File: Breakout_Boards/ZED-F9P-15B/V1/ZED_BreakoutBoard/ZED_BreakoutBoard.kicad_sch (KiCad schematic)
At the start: 15 parts, among them IC1 ZED-F9P-15B, J1 RF2-04A-T-00-50-G, J2 GPS_Conn_02x04_Top_Bottom

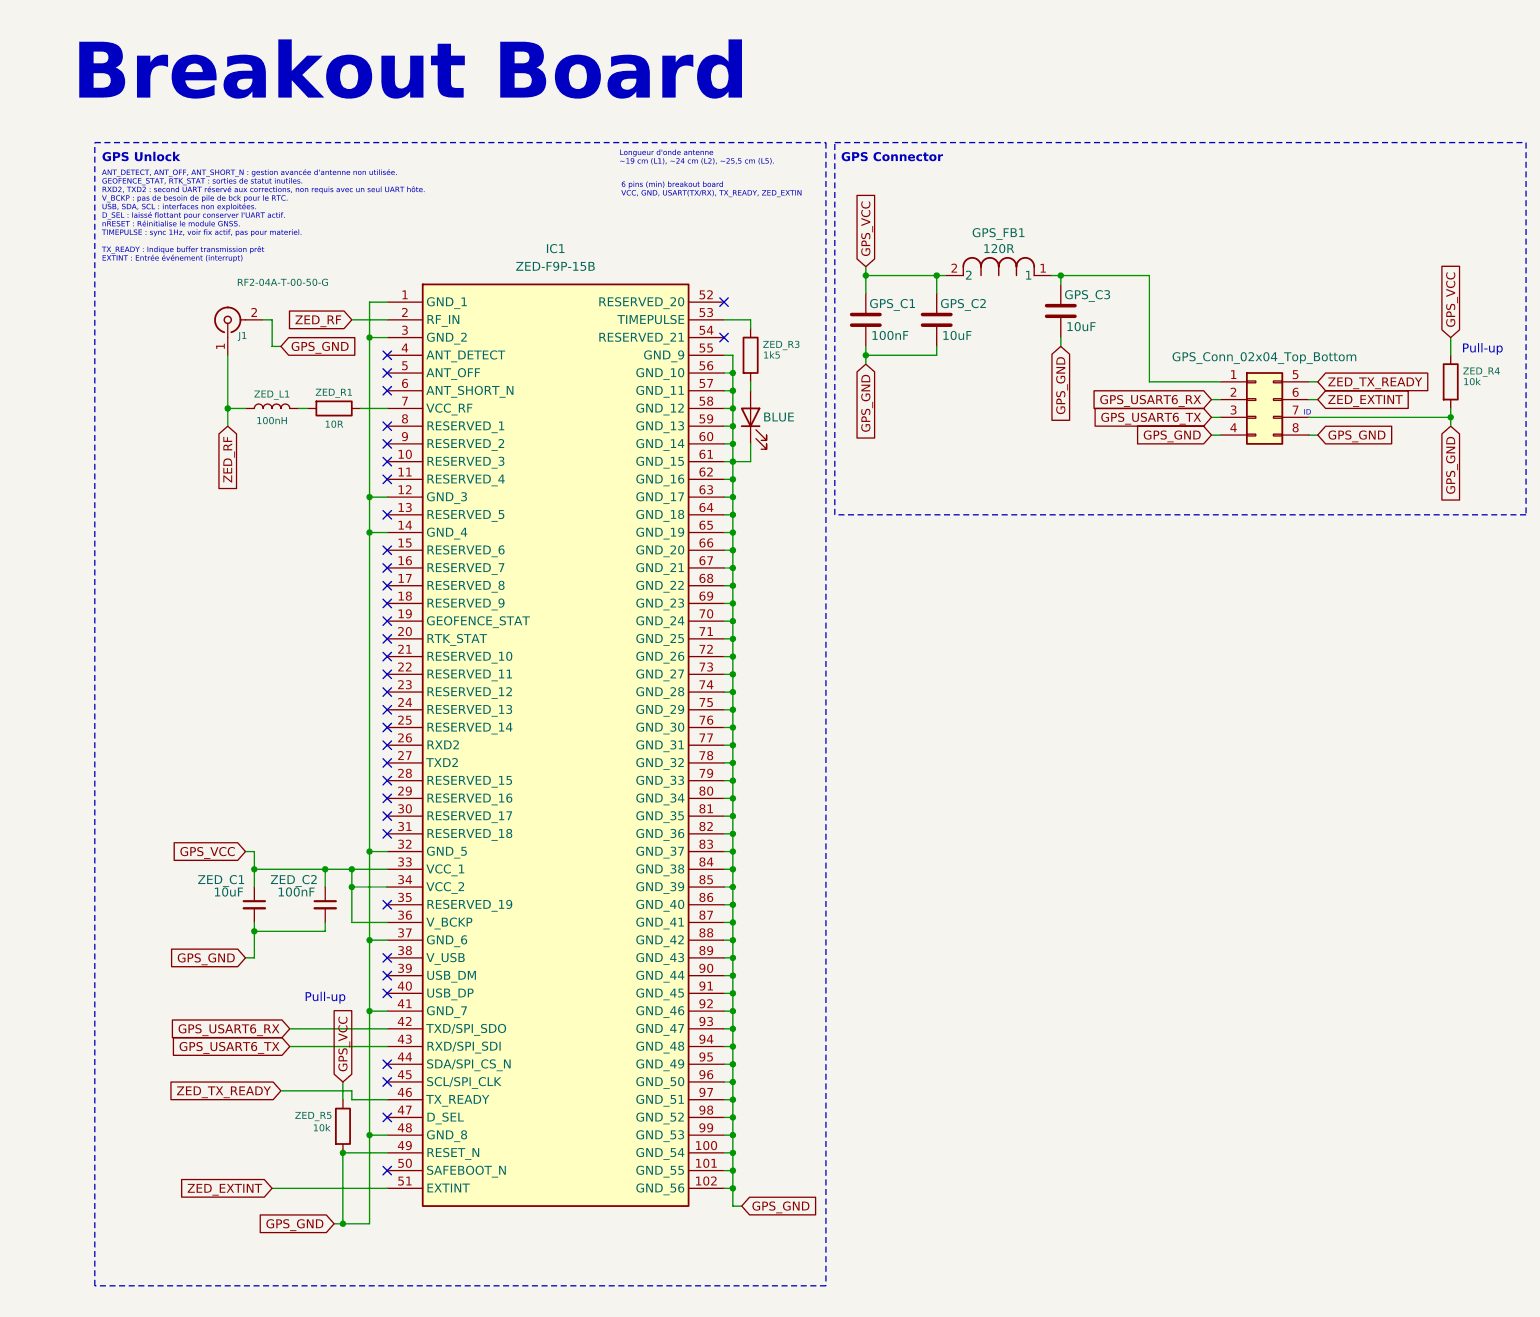
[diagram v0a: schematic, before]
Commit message: fix: pull-up -> 1 logic
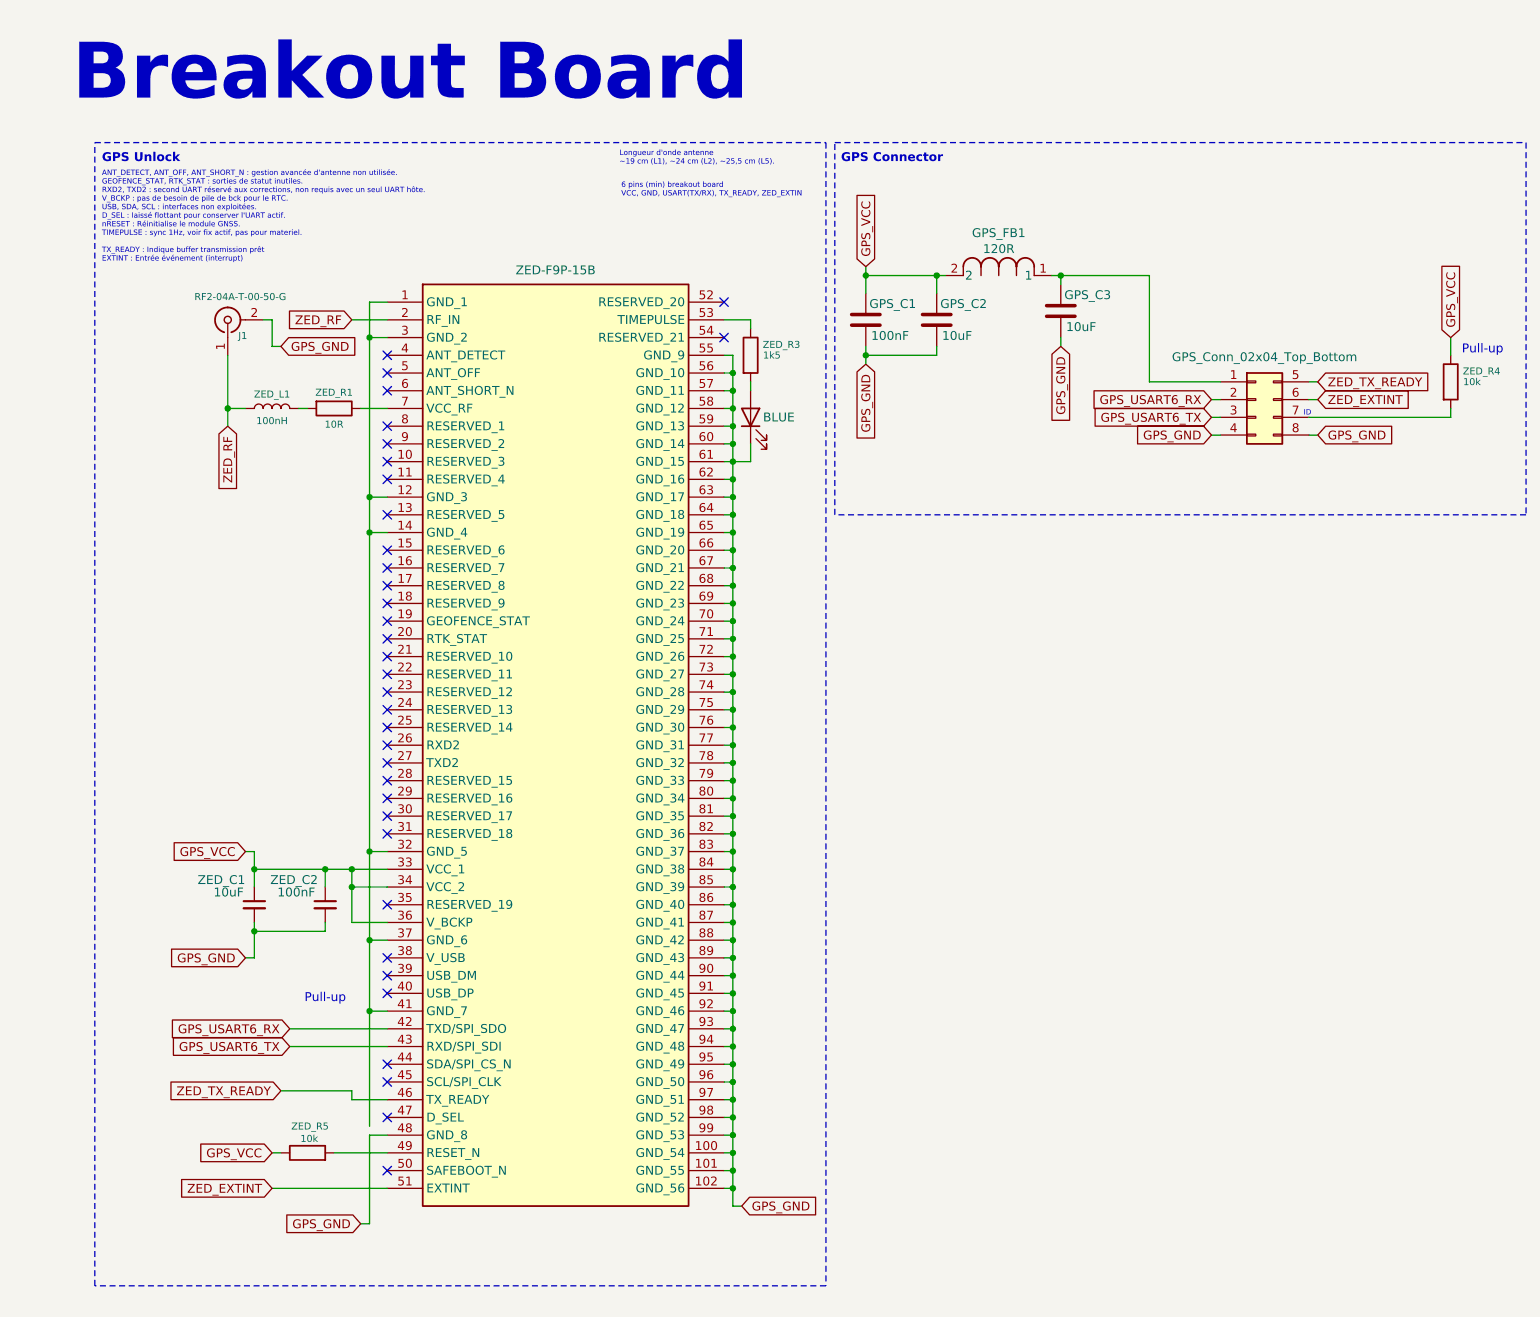
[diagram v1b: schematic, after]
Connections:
- net GPS_GND: no longer IC1.1 (GND_1), IC1.12 (GND_3), IC1.14 (GND_4), IC1.3 (GND_2), IC1.32 (GND_5), IC1.37 (GND_6), IC1.41 (GND_7), IC1.49 (RESET_N), J2.7 (Pin_7), ZED_R4.2, ZED_R5.2
- new net: J2.7 (Pin_7), ZED_R4.2
- new net: IC1.1 (GND_1), IC1.12 (GND_3), IC1.14 (GND_4), IC1.3 (GND_2), IC1.32 (GND_5), IC1.37 (GND_6), IC1.41 (GND_7)
- new net: IC1.49 (RESET_N), ZED_R5.2
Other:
- moved on the sheet: ZED_R5
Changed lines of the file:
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@@
 	)
 	(junction
-		(at 209.55 69.85)
-		(diameter 0)
-		(color 0 0 0 0)
-	)
-	(junction
 		(at 106.68 93.98)
 		(diameter 0)
@@
 	)
 	(junction
-		(at 50.8 185.42)
-		(diameter 0)
-		(color 0 0 0 0)
-	)
-	(junction
 		(at 106.68 180.34)
 		(diameter 0)
@@
 	)
 	(junction
-		(at 50.8 175.26)
-		(diameter 0)
-		(color 0 0 0 0)
-	)
-	(junction
 		(at 106.68 111.76)
 		(diameter 0)
@@
 	)
 	(junction
-		(at 54.61 172.72)
-		(diameter 0)
-		(color 0 0 0 0)
-	)
-	(junction
 		(at 38.1 134.62)
 		(diameter 0)
@@
 	(wire
 		(pts
-			(xy 106.68 73.66) (xy 106.68 76.2)
+			(xy 49.53 175.26) (xy 57.15 175.26)
 		)
 		(stroke
@@
 	(wire
 		(pts
-			(xy 57.15 53.34) (xy 54.61 53.34)
+			(xy 106.68 73.66) (xy 106.68 76.2)
 		)
 		(stroke
@@
 	(wire
 		(pts
-			(xy 125.73 60.96) (xy 125.73 62.23)
+			(xy 57.15 53.34) (xy 54.61 53.34)
 		)
 		(stroke
@@
 	(wire
 		(pts
-			(xy 105.41 96.52) (xy 106.68 96.52)
+			(xy 125.73 60.96) (xy 125.73 62.23)
 		)
 		(stroke
@@
 	(wire
 		(pts
-			(xy 153.67 58.42) (xy 153.67 59.69)
+			(xy 105.41 96.52) (xy 106.68 96.52)
 		)
 		(stroke
@@
 	(wire
 		(pts
-			(xy 54.61 86.36) (xy 54.61 132.08)
+			(xy 153.67 58.42) (xy 153.67 59.69)
 		)
 		(stroke
@@
 	(wire
 		(pts
-			(xy 105.41 127) (xy 106.68 127)
+			(xy 54.61 86.36) (xy 54.61 132.08)
 		)
 		(stroke
@@
 	(wire
 		(pts
-			(xy 50.8 175.26) (xy 50.8 185.42)
+			(xy 105.41 127) (xy 106.68 127)
 		)
 		(stroke
@@
 	(wire
 		(pts
+			(xy 40.64 175.26) (xy 41.91 175.26)
+		)
+		(stroke
+			(width 0)
+			(type default)
+		)
+	)
+	(wire
+		(pts
 			(xy 106.68 177.8) (xy 106.68 180.34)
 		)
@@
 	(wire
 		(pts
-			(xy 54.61 154.94) (xy 54.61 172.72)
+			(xy 54.61 154.94) (xy 54.61 171.45)
 		)
 		(stroke
@@
 	(wire
 		(pts
-			(xy 49.53 185.42) (xy 50.8 185.42)
-		)
-		(stroke
-			(width 0)
-			(type default)
-		)
-	)
-	(wire
-		(pts
 			(xy 43.18 160.02) (xy 57.15 160.02)
 		)
@@
 	(wire
 		(pts
-			(xy 50.8 175.26) (xy 57.15 175.26)
-		)
-		(stroke
-			(width 0)
-			(type default)
-		)
-	)
-	(wire
-		(pts
 			(xy 153.67 49.53) (xy 153.67 50.8)
 		)
@@
 	(wire
 		(pts
-			(xy 50.8 165.1) (xy 50.8 167.64)
-		)
-		(stroke
-			(width 0)
-			(type default)
-		)
-	)
-	(wire
-		(pts
 			(xy 105.41 157.48) (xy 106.68 157.48)
 		)
@@
 	(wire
 		(pts
-			(xy 209.55 69.85) (xy 209.55 71.12)
-		)
-		(stroke
-			(width 0)
-			(type default)
-		)
-	)
-	(wire
-		(pts
 			(xy 106.68 83.82) (xy 106.68 86.36)
 		)
@@
 	(wire
 		(pts
-			(xy 54.61 185.42) (xy 50.8 185.42)
+			(xy 53.34 185.42) (xy 54.61 185.42)
 		)
 		(stroke
@@
 	(global_label "GPS_VCC"
 		(shape input)
-		(at 50.8 165.1 90)
+		(at 40.64 175.26 180)
 		(fields_autoplaced yes)
 		(effects
@@
 				(size 1.27 1.27)
 			)
-			(justify left)
+			(justify right)
 		)
 		(property "Intersheetrefs" "${INTERSHEET_REFS}"
-			(at 50.8 153.7691 90)
+			(at 29.3091 175.26 0)
 			(effects
 				(font
 					(size 1.27 1.27)
 				)
-				(justify left)
+				(justify right)
 				(hide yes)
 			)
@@
 	(global_label "GPS_GND"
 		(shape input)
-		(at 49.53 185.42 180)
+		(at 53.34 185.42 180)
 		(fields_autoplaced yes)
 		(effects
@@
 		)
 		(property "Intersheetrefs" "${INTERSHEET_REFS}"
-			(at 37.9572 185.42 0)
+			(at 41.7672 185.42 0)
 			(effects
 				(font
@@
 		)
 		(property "impedance" "50ohm"
-			(at 37.846 51.054 0)
+			(at 32.512 57.15 0)
 			(effects
 				(font
@@
 	(global_label "GPS_GND"
 		(shape input)
-		(at 209.55 71.12 270)
-		(fields_autoplaced yes)
-		(effects
-			(font
-				(size 1.27 1.27)
-			)
-			(justify right)
-		)
-		(property "Intersheetrefs" "${INTERSHEET_REFS}"
-			(at 209.55 82.6928 90)
-			(effects
-				(font
-					(size 1.27 1.27)
-				)
-				(justify right)
-				(hide yes)
-			)
-		)
-	)
-	(global_label "GPS_GND"
-		(shape input)
 		(at 153.67 59.69 270)
 		(fields_autoplaced yes)
@@
 		(on_board yes)
 		(dnp no)
-		(fields_autoplaced yes)
 		(property "Reference" "IC1"
 			(at 81.28 45.72 0)
@@
 					(size 1.27 1.27)
 				)
+				(hide yes)
 			)
 		)
 		(property "Value" "ZED-F9P-15B"
-			(at 81.28 48.26 0)
+			(at 81.28 48.768 0)
 			(effects
 				(font
@@
 		)
 		(property "Value" "RF2-04A-T-00-50-G"
-			(at 48.768 50.546 90)
+			(at 42.672 52.578 90)
 			(effects
 				(font
@@
 	(symbol
 		(lib_id "Device:R")
-		(at 50.8 171.45 0)
+		(at 45.72 175.26 90)
 		(unit 1)
 		(exclude_from_sim no)
@@
 		(dnp no)
 		(property "Reference" "ZED_R5"
-			(at 49.276 169.926 0)
+			(at 48.768 171.45 90)
 			(effects
 				(font
 					(size 1 1)
 				)
-				(justify right)
+				(justify left)
 			)
 		)
 		(property "Value" "10k"
-			(at 49.022 171.704 0)
+			(at 47.244 173.228 90)
 			(effects
 				(font
 					(size 1 1)
 				)
-				(justify right)
+				(justify left)
 			)
 		)
 		(property "Footprint" "Resistor_SMD:R_0603_1608Metric"
-			(at 49.022 171.45 90)
+			(at 45.72 177.038 90)
 			(effects
 				(font
@@
 		)
 		(property "Datasheet" "~"
-			(at 50.8 171.45 0)
+			(at 45.72 175.26 0)
 			(effects
 				(font
@@
 		)
 		(property "Description" ""
-			(at 50.8 171.45 0)
+			(at 45.72 175.26 0)
 			(effects
 				(font

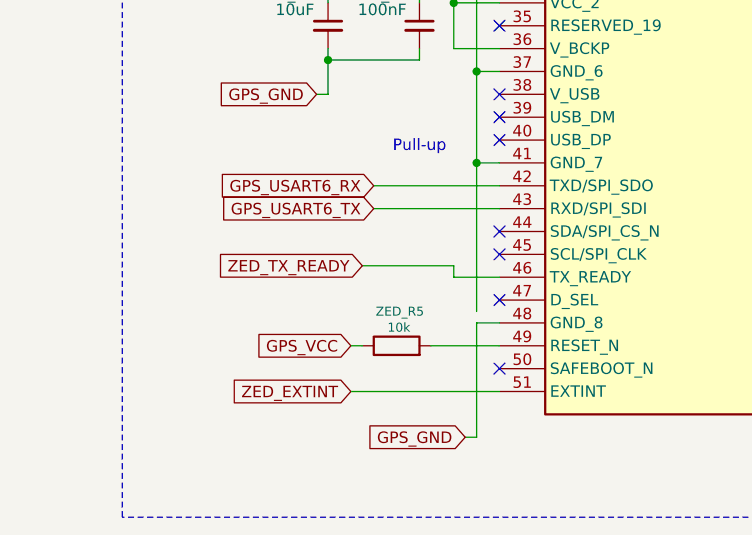
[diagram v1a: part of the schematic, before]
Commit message: fix: gnd connection, pcb approximative edge
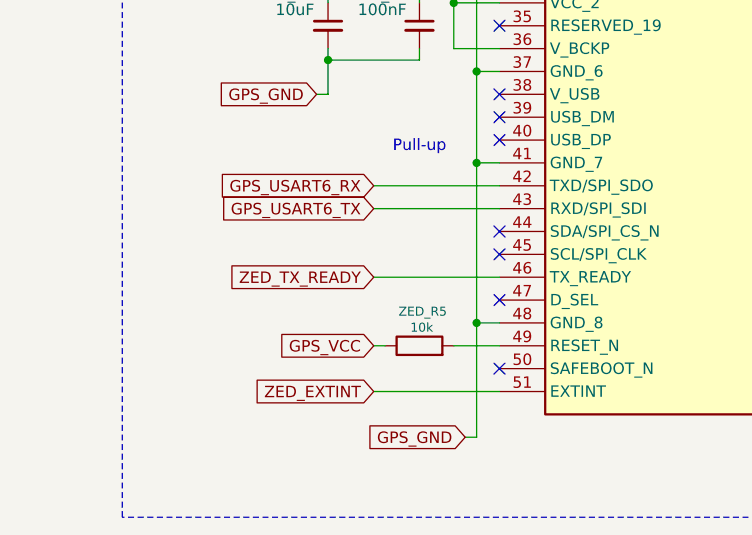
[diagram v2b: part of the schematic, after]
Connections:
- net GPS_GND: now also IC1.1 (GND_1), IC1.12 (GND_3), IC1.14 (GND_4), IC1.3 (GND_2), IC1.32 (GND_5), IC1.37 (GND_6), IC1.41 (GND_7)
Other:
- moved on the sheet: ZED_R5
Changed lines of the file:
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@@
 	)
 	(junction
+		(at 54.61 172.72)
+		(diameter 0)
+		(color 0 0 0 0)
+	)
+	(junction
 		(at 106.68 180.34)
 		(diameter 0)
@@
 	(wire
 		(pts
-			(xy 49.53 175.26) (xy 57.15 175.26)
+			(xy 52.07 175.26) (xy 57.15 175.26)
 		)
 		(stroke
@@
 	(wire
 		(pts
-			(xy 52.07 167.64) (xy 57.15 167.64)
-		)
-		(stroke
-			(width 0)
-			(type default)
-		)
-	)
-	(wire
-		(pts
 			(xy 189.23 72.39) (xy 190.5 72.39)
 		)
@@
 	(wire
 		(pts
-			(xy 40.64 175.26) (xy 41.91 175.26)
+			(xy 43.18 175.26) (xy 44.45 175.26)
 		)
 		(stroke
@@
 	(wire
 		(pts
-			(xy 54.61 154.94) (xy 54.61 171.45)
+			(xy 54.61 154.94) (xy 54.61 172.72)
 		)
 		(stroke
@@
 	(wire
 		(pts
-			(xy 52.07 166.37) (xy 52.07 167.64)
-		)
-		(stroke
-			(width 0)
-			(type default)
-		)
-	)
-	(wire
-		(pts
 			(xy 135.89 60.96) (xy 135.89 59.69)
 		)
@@
 	(wire
 		(pts
-			(xy 41.91 166.37) (xy 52.07 166.37)
+			(xy 43.18 167.64) (xy 57.15 167.64)
 		)
 		(stroke
@@
 	(wire
 		(pts
-			(xy 40.64 180.34) (xy 57.15 180.34)
+			(xy 43.18 180.34) (xy 57.15 180.34)
 		)
 		(stroke
@@
 	(global_label "GPS_VCC"
 		(shape input)
-		(at 40.64 175.26 180)
+		(at 43.18 175.26 180)
 		(fields_autoplaced yes)
 		(effects
@@
 		)
 		(property "Intersheetrefs" "${INTERSHEET_REFS}"
-			(at 29.3091 175.26 0)
+			(at 31.8491 175.26 0)
 			(effects
 				(font
@@
 	(global_label "ZED_EXTINT"
 		(shape input)
-		(at 40.64 180.34 180)
+		(at 43.18 180.34 180)
 		(fields_autoplaced yes)
 		(effects
@@
 		)
 		(property "Intersheetrefs" "${INTERSHEET_REFS}"
-			(at 26.8297 180.34 0)
+			(at 29.3697 180.34 0)
 			(effects
 				(font
@@
 	(global_label "ZED_TX_READY"
 		(shape input)
-		(at 41.91 166.37 180)
+		(at 43.18 167.64 180)
 		(fields_autoplaced yes)
 		(effects
@@
 		)
 		(property "Intersheetrefs" "${INTERSHEET_REFS}"
-			(at 25.3178 166.37 0)
+			(at 26.5878 167.64 0)
 			(effects
 				(font
@@
 	(symbol
 		(lib_id "Device:R")
-		(at 45.72 175.26 90)
+		(at 48.26 175.26 90)
 		(unit 1)
 		(exclude_from_sim no)
@@
 		(dnp no)
 		(property "Reference" "ZED_R5"
-			(at 48.768 171.45 90)
+			(at 51.308 171.45 90)
 			(effects
 				(font
@@
 		)
 		(property "Value" "10k"
-			(at 47.244 173.228 90)
+			(at 49.784 173.228 90)
 			(effects
 				(font
@@
 		)
 		(property "Footprint" "Resistor_SMD:R_0603_1608Metric"
-			(at 45.72 177.038 90)
+			(at 48.26 177.038 90)
 			(effects
 				(font
@@
 		)
 		(property "Datasheet" "~"
-			(at 45.72 175.26 0)
+			(at 48.26 175.26 0)
 			(effects
 				(font
@@
 		)
 		(property "Description" ""
-			(at 45.72 175.26 0)
+			(at 48.26 175.26 0)
 			(effects
 				(font
